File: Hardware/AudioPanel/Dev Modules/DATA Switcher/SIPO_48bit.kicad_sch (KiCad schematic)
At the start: 14 parts, among them U808 SN74LV595ARGYR, U809 SN74LV595ARGYR, U810 SN74LV595ARGYR, U811 SN74LV595ARGYR, U812 SN74LV595ARGYR, U813 SN74LV595ARGYR

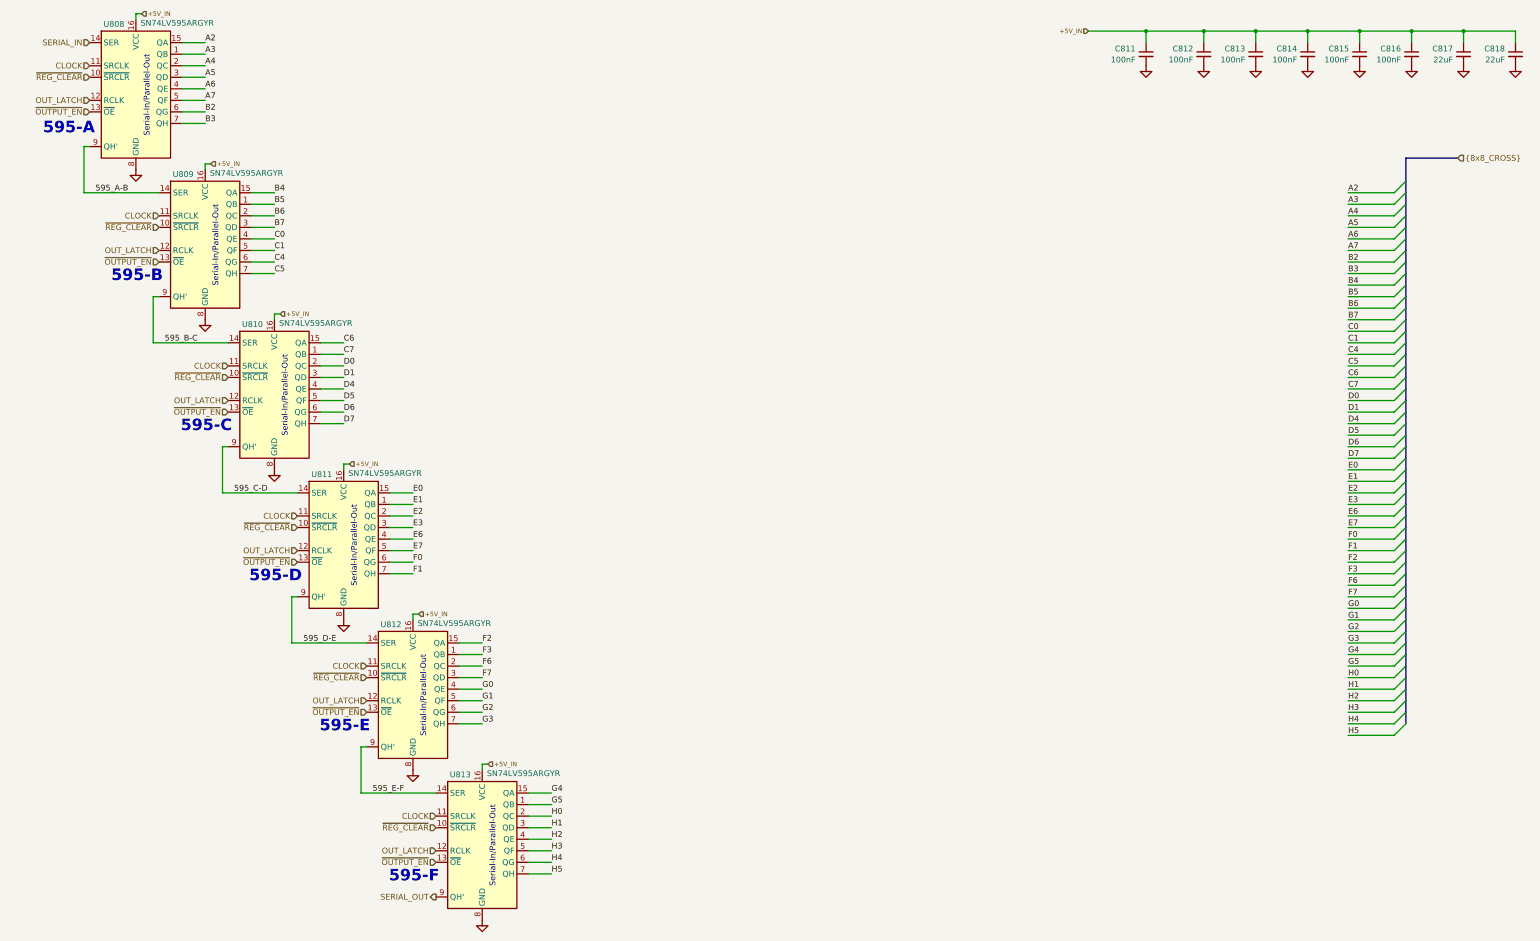
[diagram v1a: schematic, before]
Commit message: Adjusted I2C addresses and component identifiers
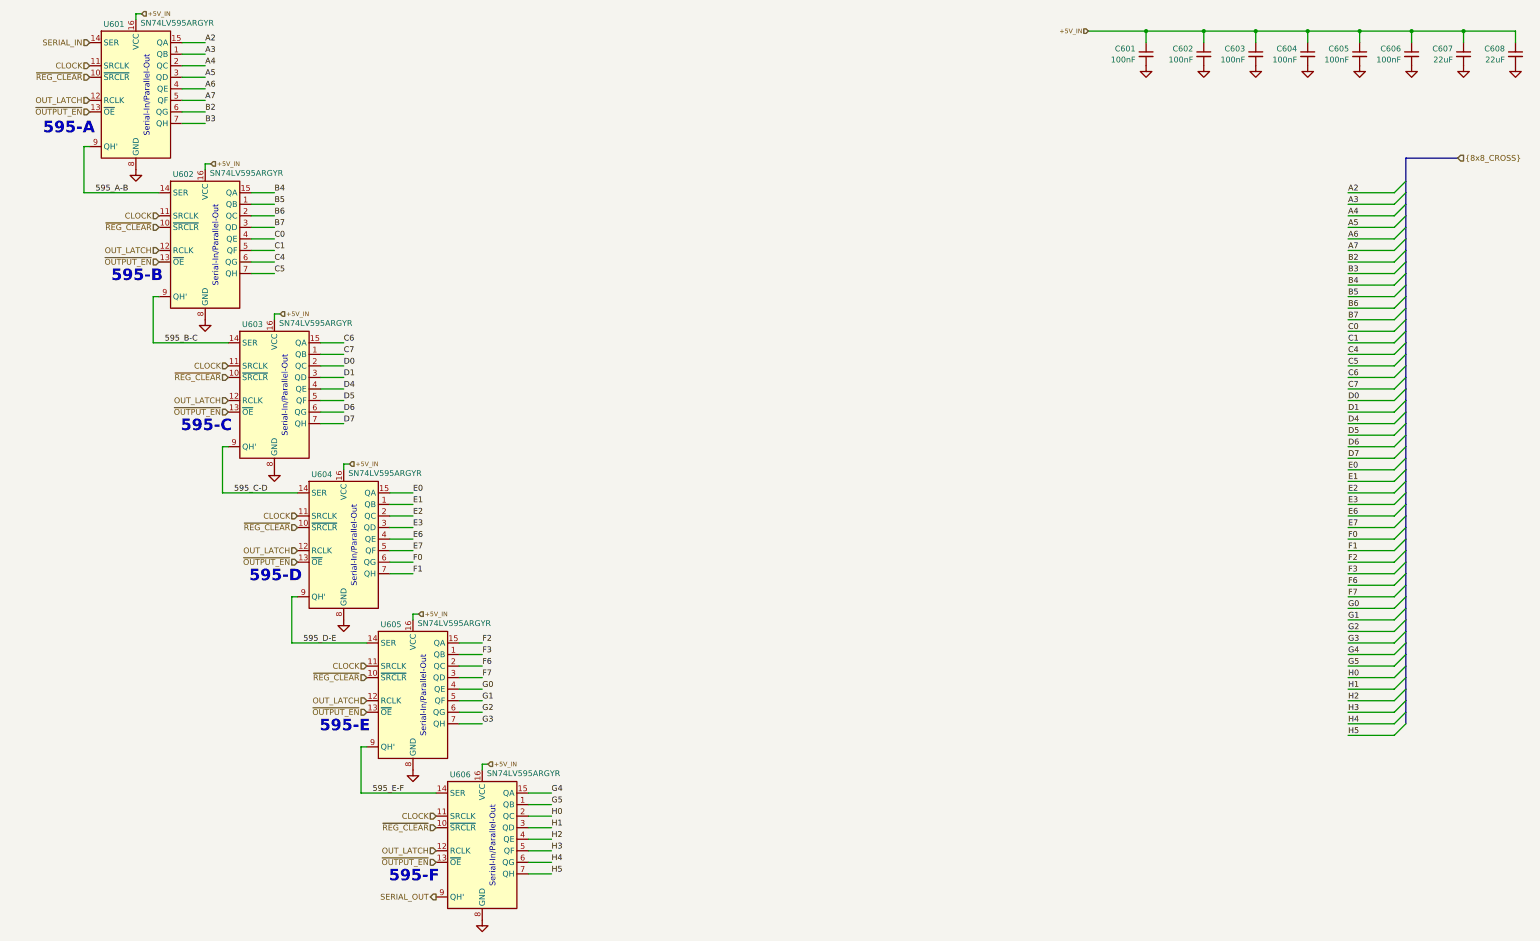
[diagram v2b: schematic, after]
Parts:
- removed C811, C812: 100nF, Capacitor_SMD:C_0402_1005Metric, symbol Device:C_Small
- removed C818: 22uF, Capacitor_SMD:C_0603_1608Metric, symbol Device:C_Small
- removed U808: SN74LV595ARGYR, Libraries:RGY16_2P55X2P05, symbol 74xx:74HC595
- added C601, C602: 100nF, Capacitor_SMD:C_0402_1005Metric, symbol Device:C_Small
- added C608: 22uF, Capacitor_SMD:C_0603_1608Metric, symbol Device:C_Small
- added U601: SN74LV595ARGYR, Libraries:RGY16_2P55X2P05, symbol 74xx:74HC595
- renumbered C813 to C603, C814 to C604, C815 to C605, C816 to C606, C817 to C607, U809 to U602, U810 to U603, U811 to U604, U812 to U605, U813 to U606
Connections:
- net +5V_IN: now also C601.1, C602.1, C608.1, U601.16 (VCC)
- net 595_A-B: now also U601.9 (QH')
- net A2: now also U601.15 (QA)
- net A3: now also U601.1 (QB)
- net A4: now also U601.2 (QC)
- net A5: now also U601.3 (QD)
- net A6: now also U601.4 (QE)
- net A7: now also U601.5 (QF)
- net B2: now also U601.6 (QG)
- net B3: now also U601.7 (QH)
- net CLOCK: now also U601.11 (SRCLK)
- net GND: now also C601.2, C602.2, C608.2, U601.8 (GND)
- net OUT_LATCH: now also U601.12 (RCLK)
- net SERIAL_IN: now also U601.14 (SER)
- net ~{OUTPUT_EN}: now also U601.13 (~{OE})
- net ~{REG_CLEAR}: now also U601.10 (~{SRCLR})
